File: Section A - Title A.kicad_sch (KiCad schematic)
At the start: 1 part, among them U1 XIAO ESP32C6

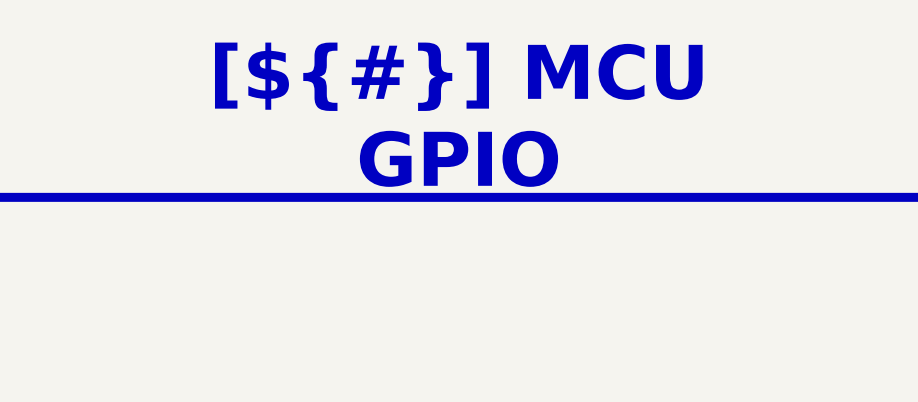
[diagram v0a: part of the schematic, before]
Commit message: [SCHEMATICS] Ajout de convertisseur + autres
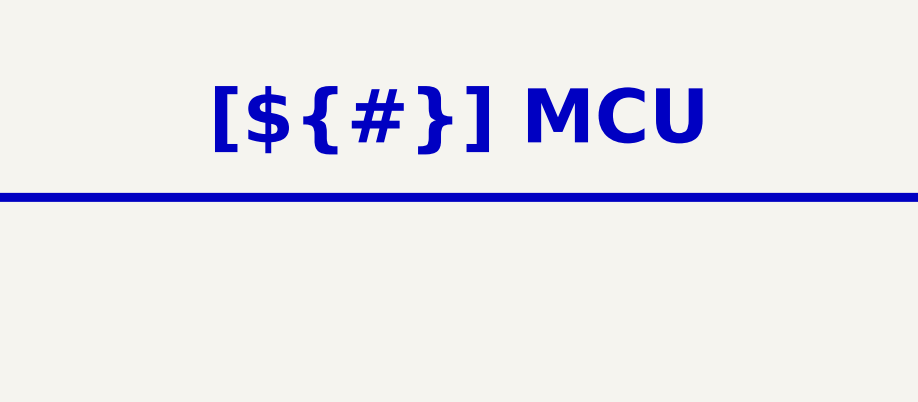
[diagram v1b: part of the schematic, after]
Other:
- title: MCU GPIO -> MCU
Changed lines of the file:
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@@
 	(paper "A4")
 	(title_block
-		(title "MCU GPIO")
+		(title "MCU")
 		(date "2025-01-12")
 		(rev "${REVISION}")
@@
 			)
 		)
+		(property "Config" ""
+			(at 144.78 78.74 0)
+			(hide yes)
+			(show_name no)
+			(do_not_autoplace no)
+			(effects
+				(font
+					(size 1.27 1.27)
+				)
+			)
+		)
+		(property "Manufacturer Part Number" ""
+			(at 144.78 78.74 0)
+			(hide yes)
+			(show_name no)
+			(do_not_autoplace no)
+			(effects
+				(font
+					(size 1.27 1.27)
+				)
+			)
+		)
